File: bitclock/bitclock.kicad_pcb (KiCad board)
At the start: 2 copper layers, 11 parts, among them IC1 ATTINY13-S, P1 USB_OTG, SW1 Hour, SW2 Minute, U1 TA23-11EWA, U2 TM1637

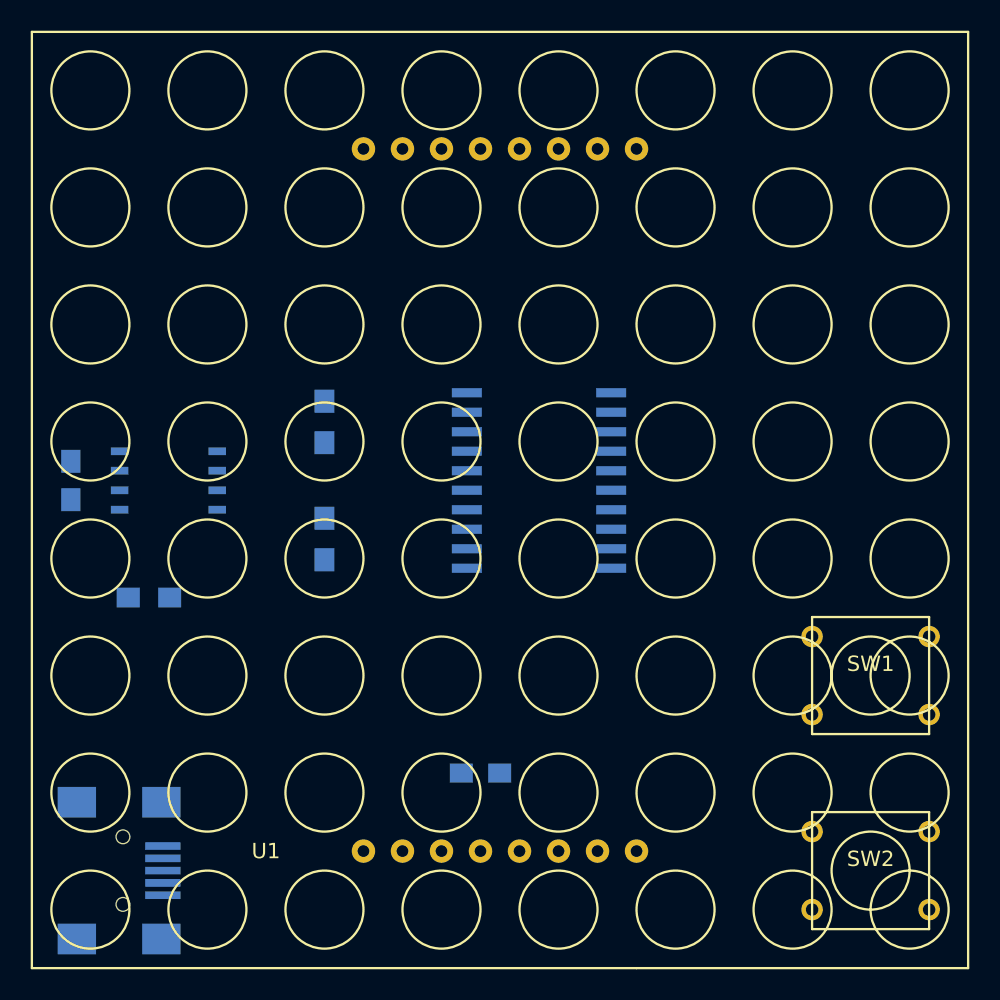
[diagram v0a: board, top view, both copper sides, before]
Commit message: bitclock: pcb trace started
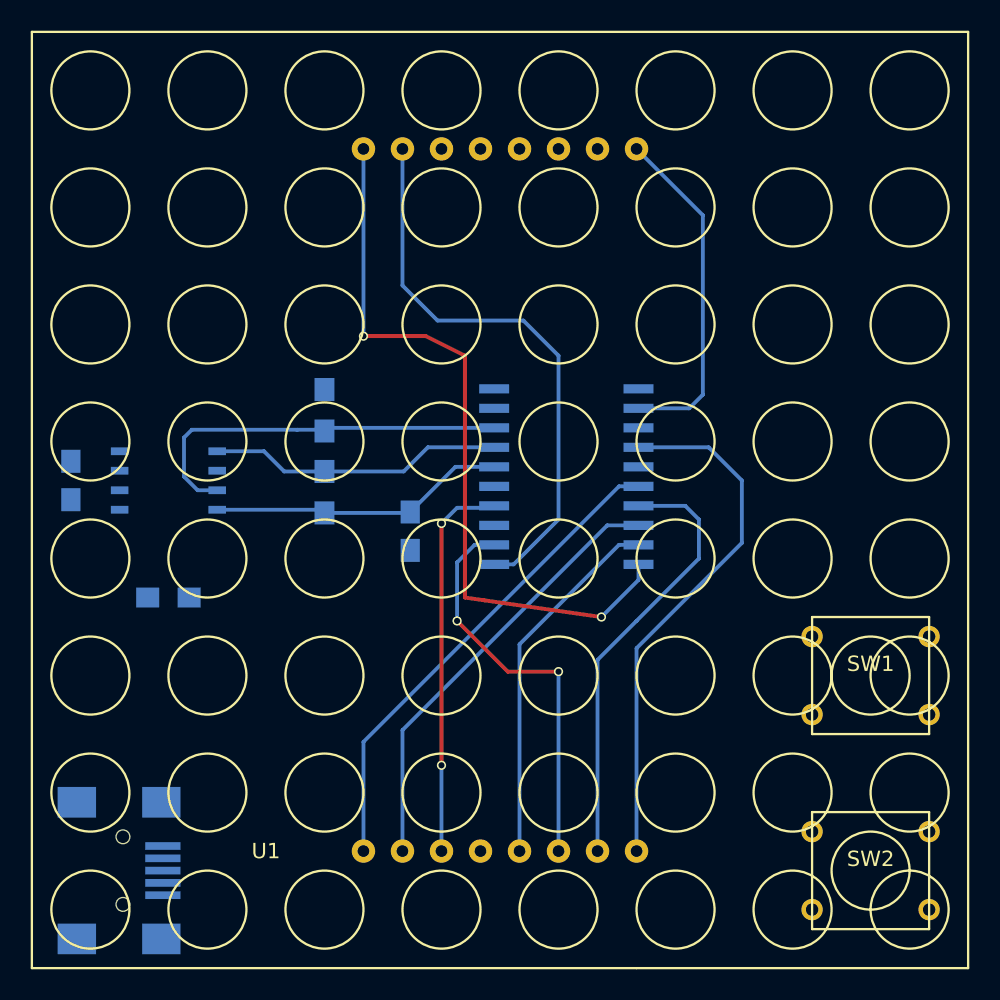
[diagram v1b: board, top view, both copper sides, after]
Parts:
- moved C1 16.4 mm to (141.5, 83.3), turned to 270 degrees
- moved R2 3.05 mm to (135.9, 80.8)
- moved U2 1.80 mm to (151.6, 79.8)
- moved R3 1.27 mm to (125.7, 87.6)
- moved R1 0.76 mm to (135.9, 75.4)
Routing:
- net COM-AN6: track 0.00 -> 48.3 mm, vias 0 -> 2
- net COM-AN5: track 0.00 -> 37.0 mm
- net SEG3: track 0.00 -> 34.6 mm
- net SEG5: track 0.00 -> 31.9 mm
- net SEG7: track 0.00 -> 28.8 mm
- net SEG6: track 0.00 -> 28.6 mm
- net COM-AN4: track 0.00 -> 26.4 mm, vias 0 -> 2
- net SCL: track 0.00 -> 25.6 mm
- net COM-AN2: track 0.00 -> 25.2 mm, vias 0 -> 2
- net SEG8: track 0.00 -> 23.9 mm
- net SEG1: track 0.00 -> 22.3 mm
- net +5V: track 0.00 -> 19.4 mm
- net SDA: track 0.00 -> 19.2 mm

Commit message: bitclock: done tracing pcb
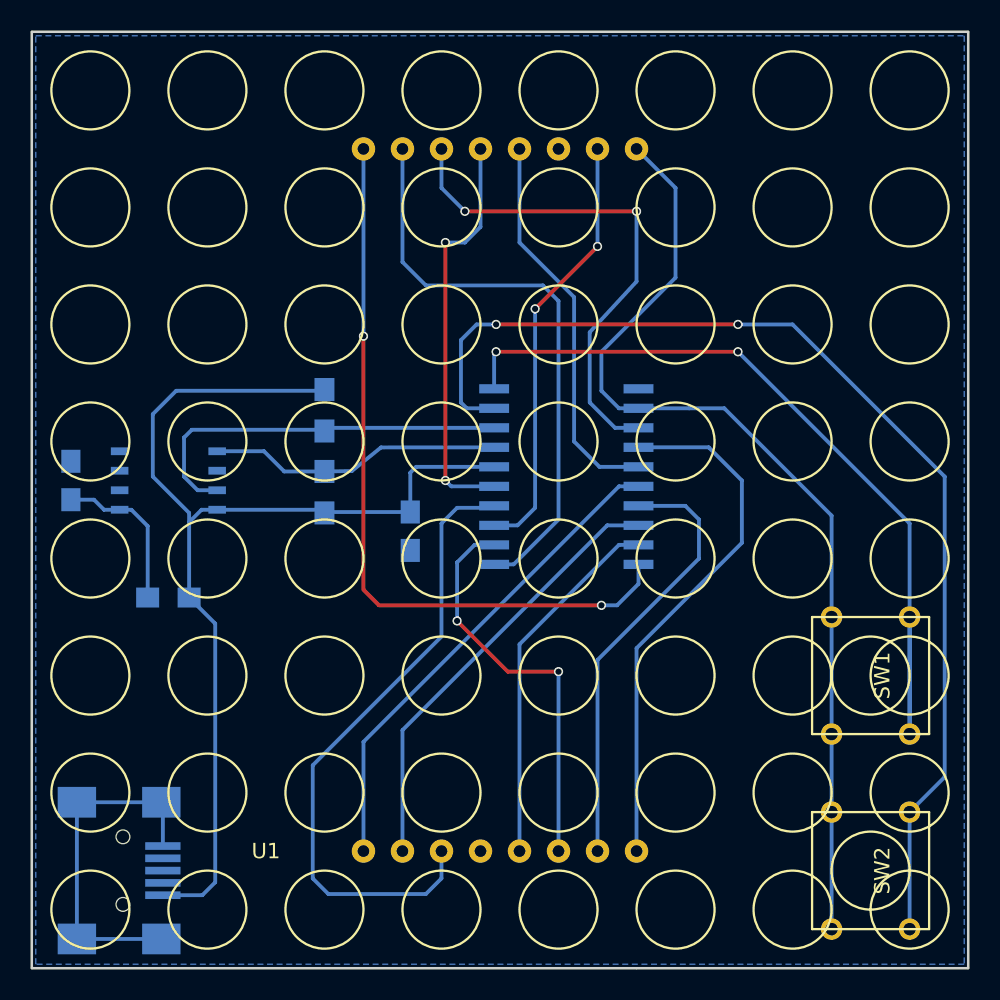
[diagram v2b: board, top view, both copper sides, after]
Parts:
- turned SW1 to 270 degrees
- turned SW2 to 270 degrees
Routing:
- net Net-(SW2-Pad1): track 0.00 -> 72.8 mm, vias 0 -> 2
- net Net-(SW1-Pad1): track 0.00 -> 55.4 mm, vias 0 -> 2
- net +5V: track 19.4 -> 70.8 mm
- net SEG1: track 22.3 -> 64.1 mm
- net SEG2: track 0.00 -> 33.4 mm, vias 0 -> 2
- net COM-AN3: track 0.00 -> 28.2 mm, vias 0 -> 2
- net COM-AN1: track 0.00 -> 26.6 mm, vias 0 -> 2
- net SEG4: track 0.00 -> 25.7 mm
- net GND: track 0.00 -> 22.8 mm
- net COM-AN2: track 25.2 -> 41.5 mm, vias 2 -> 0
- net Net-(C2-Pad1): track 0.00 -> 10.4 mm
- net COM-AN5: track 37.0 -> 38.2 mm
- net COM-AN6: track 48.3 -> 48.9 mm
- added copper zone on B.Cu, net GND
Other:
- board outline added: 61 x 61 mm

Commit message: bitclock: pcb: wider traces, larger vias
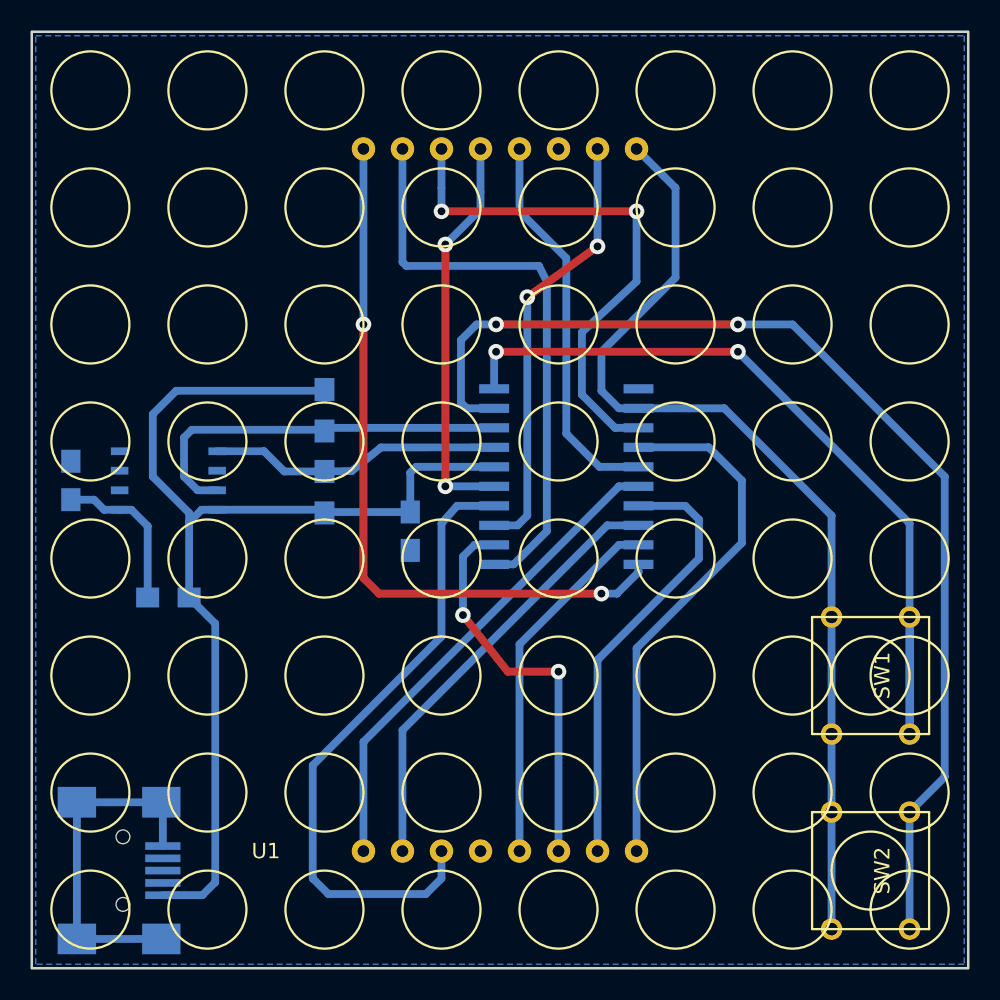
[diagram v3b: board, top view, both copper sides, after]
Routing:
- net COM-AN6: track 48.9 -> 47.4 mm
- net SEG2: track 33.4 -> 34.8 mm
- net COM-AN1: track 26.6 -> 26.1 mm, vias 2 -> 3
- net COM-AN4: track 26.4 -> 25.8 mm
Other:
- net class Default: clearance 0.2 -> 0.254; trace_width 0.25 -> 0.508; via_dia 0.6 -> 1.016; via_drill 0.4 -> 0.508
- rule trace_clearance: 0.2 -> 0.254

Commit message: lora1278 breakout: added
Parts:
- SW1, SW2: moved to B.Cu
- turned SW1 to 90 degrees
- turned SW2 to 90 degrees
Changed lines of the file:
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@@
     (links 42)
     (no_connects 0)
-    (area 116.155 50.524999 178.075001 113.4843)
+    (area 116.764999 50.724999 177.875001 111.835001)
     (thickness 1.6)
     (drawings 5)
@@
     )
   )
-  (module Buttons_Switches_ThroughHole:SW_PUSH_SMALL (layer F.Cu)
-    (at 171.45 92.71 270)
-    (fp_text reference SW1 (at 0 -0.762 270) (layer F.SilkS)
-      (effects (font (size 1 1) (thickness 0.15)))
-    )
-    (fp_text value Hour (at 0 1.016 270) (layer F.Fab)
-      (effects (font (size 1 1) (thickness 0.15)))
-    )
-    (fp_circle (center 0 0) (end 0 -2.54) (layer F.SilkS) (width 0.15))
-    (fp_line (start -3.81 -3.81) (end 3.81 -3.81) (layer F.SilkS) (width 0.15))
-    (fp_line (start 3.81 -3.81) (end 3.81 3.81) (layer F.SilkS) (width 0.15))
-    (fp_line (start 3.81 3.81) (end -3.81 3.81) (layer F.SilkS) (width 0.15))
-    (fp_line (start -3.81 -3.81) (end -3.81 3.81) (layer F.SilkS) (width 0.15))
-    (pad 1 thru_hole circle (at 3.81 -2.54 270) (size 1.397 1.397) (drill 0.8128) (layers *.Cu *.Mask F.SilkS)
+  (module Buttons_Switches_ThroughHole:SW_PUSH_SMALL (layer B.Cu)
+    (at 171.45 92.71 90)
+    (fp_text reference SW1 (at 0 0.762 90) (layer B.SilkS)
+      (effects (font (size 1 1) (thickness 0.15)) (justify mirror))
+    )
+    (fp_text value Hour (at 0 -1.016 90) (layer B.Fab)
+      (effects (font (size 1 1) (thickness 0.15)) (justify mirror))
+    )
+    (fp_circle (center 0 0) (end 0 2.54) (layer B.SilkS) (width 0.15))
+    (fp_line (start -3.81 3.81) (end 3.81 3.81) (layer B.SilkS) (width 0.15))
+    (fp_line (start 3.81 3.81) (end 3.81 -3.81) (layer B.SilkS) (width 0.15))
+    (fp_line (start 3.81 -3.81) (end -3.81 -3.81) (layer B.SilkS) (width 0.15))
+    (fp_line (start -3.81 3.81) (end -3.81 -3.81) (layer B.SilkS) (width 0.15))
+    (pad 1 thru_hole circle (at 3.81 2.54 90) (size 1.397 1.397) (drill 0.8128) (layers *.Cu *.Mask B.SilkS)
       (net 12 "Net-(SW1-Pad1)"))
-    (pad 2 thru_hole circle (at 3.81 2.54 270) (size 1.397 1.397) (drill 0.8128) (layers *.Cu *.Mask F.SilkS)
+    (pad 2 thru_hole circle (at 3.81 -2.54 90) (size 1.397 1.397) (drill 0.8128) (layers *.Cu *.Mask B.SilkS)
       (net 13 SEG1))
-    (pad 1 thru_hole circle (at -3.81 -2.54 270) (size 1.397 1.397) (drill 0.8128) (layers *.Cu *.Mask F.SilkS)
+    (pad 1 thru_hole circle (at -3.81 2.54 90) (size 1.397 1.397) (drill 0.8128) (layers *.Cu *.Mask B.SilkS)
       (net 12 "Net-(SW1-Pad1)"))
-    (pad 2 thru_hole circle (at -3.81 2.54 270) (size 1.397 1.397) (drill 0.8128) (layers *.Cu *.Mask F.SilkS)
+    (pad 2 thru_hole circle (at -3.81 -2.54 90) (size 1.397 1.397) (drill 0.8128) (layers *.Cu *.Mask B.SilkS)
       (net 13 SEG1))
   )
-  (module Buttons_Switches_ThroughHole:SW_PUSH_SMALL (layer F.Cu)
-    (at 171.45 105.41 270)
-    (fp_text reference SW2 (at 0 -0.762 270) (layer F.SilkS)
-      (effects (font (size 1 1) (thickness 0.15)))
-    )
-    (fp_text value Minute (at 0 1.016 270) (layer F.Fab)
-      (effects (font (size 1 1) (thickness 0.15)))
-    )
-    (fp_circle (center 0 0) (end 0 -2.54) (layer F.SilkS) (width 0.15))
-    (fp_line (start -3.81 -3.81) (end 3.81 -3.81) (layer F.SilkS) (width 0.15))
-    (fp_line (start 3.81 -3.81) (end 3.81 3.81) (layer F.SilkS) (width 0.15))
-    (fp_line (start 3.81 3.81) (end -3.81 3.81) (layer F.SilkS) (width 0.15))
-    (fp_line (start -3.81 -3.81) (end -3.81 3.81) (layer F.SilkS) (width 0.15))
-    (pad 1 thru_hole circle (at 3.81 -2.54 270) (size 1.397 1.397) (drill 0.8128) (layers *.Cu *.Mask F.SilkS)
+  (module Buttons_Switches_ThroughHole:SW_PUSH_SMALL (layer B.Cu)
+    (at 171.45 105.41 90)
+    (fp_text reference SW2 (at 0 0.762 90) (layer B.SilkS)
+      (effects (font (size 1 1) (thickness 0.15)) (justify mirror))
+    )
+    (fp_text value Minute (at 0 -1.016 90) (layer B.Fab)
+      (effects (font (size 1 1) (thickness 0.15)) (justify mirror))
+    )
+    (fp_circle (center 0 0) (end 0 2.54) (layer B.SilkS) (width 0.15))
+    (fp_line (start -3.81 3.81) (end 3.81 3.81) (layer B.SilkS) (width 0.15))
+    (fp_line (start 3.81 3.81) (end 3.81 -3.81) (layer B.SilkS) (width 0.15))
+    (fp_line (start 3.81 -3.81) (end -3.81 -3.81) (layer B.SilkS) (width 0.15))
+    (fp_line (start -3.81 3.81) (end -3.81 -3.81) (layer B.SilkS) (width 0.15))
+    (pad 1 thru_hole circle (at 3.81 2.54 90) (size 1.397 1.397) (drill 0.8128) (layers *.Cu *.Mask B.SilkS)
       (net 14 "Net-(SW2-Pad1)"))
-    (pad 2 thru_hole circle (at 3.81 2.54 270) (size 1.397 1.397) (drill 0.8128) (layers *.Cu *.Mask F.SilkS)
+    (pad 2 thru_hole circle (at 3.81 -2.54 90) (size 1.397 1.397) (drill 0.8128) (layers *.Cu *.Mask B.SilkS)
       (net 13 SEG1))
-    (pad 1 thru_hole circle (at -3.81 -2.54 270) (size 1.397 1.397) (drill 0.8128) (layers *.Cu *.Mask F.SilkS)
+    (pad 1 thru_hole circle (at -3.81 2.54 90) (size 1.397 1.397) (drill 0.8128) (layers *.Cu *.Mask B.SilkS)
       (net 14 "Net-(SW2-Pad1)"))
-    (pad 2 thru_hole circle (at -3.81 2.54 270) (size 1.397 1.397) (drill 0.8128) (layers *.Cu *.Mask F.SilkS)
+    (pad 2 thru_hole circle (at -3.81 -2.54 90) (size 1.397 1.397) (drill 0.8128) (layers *.Cu *.Mask B.SilkS)
       (net 13 SEG1))
   )
